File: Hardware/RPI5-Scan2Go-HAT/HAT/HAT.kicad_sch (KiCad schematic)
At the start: 30 parts, among them J1 RPi_GPIO, J10 Screw_Terminal_01x02, J11 Screw_Terminal_01x02, J12 Screw_Terminal_01x02, J13 Screw_Terminal_01x02, J14 Screw_Terminal_01x02, J15 Jack-DC 5V, J16 Screw_Terminal_01x02, J17 Screw_Terminal_01x02, J18 Screw_Terminal_01x02, J2 Screw_Terminal_01x03, J20 Screw_Terminal_01x05, J21 Screw_Terminal_01x06, J3 Conn_01x14_Socket, J4 Screw_Terminal_01x03, J5 Screw_Terminal_01x03, J6 Screw_Terminal_01x03, J7 Screw_Terminal_01x04, J8 Screw_Terminal_01x04, J9 Screw_Terminal_01x02, Q1 DMG2305UX, U1 Pico

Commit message: added footprints
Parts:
- J10, J11, J12, J13, J14, J16, J17, J18, J9: footprint (none) -> TerminalBlock:TerminalBlock_bornier-2_P5.08mm
- J2, J4, J5, J6: footprint (none) -> TerminalBlock:TerminalBlock_bornier-3_P5.08mm
- J20: footprint (none) -> TerminalBlock:TerminalBlock_bornier-5_P5.08mm
- J21: footprint (none) -> TerminalBlock:TerminalBlock_bornier-6_P5.08mm
- J7, J8: footprint (none) -> TerminalBlock:TerminalBlock_bornier-4_P5.08mm
- JP1, JP2: footprint (none) -> Jumper:SolderJumper-2_P1.3mm_Open_TrianglePad1.0x1.5mm
- TP1: footprint (none) -> TestPoint:TestPoint_Pad_2.0x2.0mm
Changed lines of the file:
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@@
 			)
 		)
-		(property "Footprint" ""
+		(property "Footprint" "TerminalBlock:TerminalBlock_bornier-6_P5.08mm"
 			(at 284.48 64.77 0)
 			(effects
@@
 			)
 		)
-		(property "Footprint" ""
+		(property "Footprint" "TerminalBlock:TerminalBlock_bornier-3_P5.08mm"
 			(at 198.12 88.9 0)
 			(effects
@@
 			)
 		)
-		(property "Footprint" ""
+		(property "Footprint" "TerminalBlock:TerminalBlock_bornier-2_P5.08mm"
 			(at 271.78 143.51 0)
 			(effects
@@
 			)
 		)
-		(property "Footprint" ""
+		(property "Footprint" "TerminalBlock:TerminalBlock_bornier-3_P5.08mm"
 			(at 198.12 116.84 0)
 			(effects
@@
 			)
 		)
-		(property "Footprint" ""
+		(property "Footprint" "TerminalBlock:TerminalBlock_bornier-4_P5.08mm"
 			(at 198.12 58.42 0)
 			(effects
@@
 			)
 		)
-		(property "Footprint" ""
+		(property "Footprint" "TerminalBlock:TerminalBlock_bornier-2_P5.08mm"
 			(at 229.87 143.51 0)
 			(effects
@@
 			)
 		)
-		(property "Footprint" ""
+		(property "Footprint" "TerminalBlock:TerminalBlock_bornier-3_P5.08mm"
 			(at 198.12 68.58 0)
 			(effects
@@
 			)
 		)
-		(property "Footprint" ""
+		(property "Footprint" "TestPoint:TestPoint_Pad_2.0x2.0mm"
 			(at 323.85 120.65 0)
 			(effects
@@
 			)
 		)
-		(property "Footprint" ""
+		(property "Footprint" "TerminalBlock:TerminalBlock_bornier-2_P5.08mm"
 			(at 294.64 143.51 0)
 			(effects
@@
 			)
 		)
-		(property "Footprint" ""
+		(property "Footprint" "TerminalBlock:TerminalBlock_bornier-3_P5.08mm"
 			(at 198.12 78.74 0)
 			(effects
@@
 			)
 		)
-		(property "Footprint" ""
+		(property "Footprint" "TerminalBlock:TerminalBlock_bornier-2_P5.08mm"
 			(at 237.49 143.51 0)
 			(effects
@@
 			)
 		)
-		(property "Footprint" ""
+		(property "Footprint" "TerminalBlock:TerminalBlock_bornier-2_P5.08mm"
 			(at 247.65 143.51 0)
 			(effects
@@
 			)
 		)
-		(property "Footprint" ""
+		(property "Footprint" "TerminalBlock:TerminalBlock_bornier-4_P5.08mm"
 			(at 198.12 104.14 0)
 			(effects
@@
 			)
 		)
-		(property "Footprint" ""
+		(property "Footprint" "TerminalBlock:TerminalBlock_bornier-2_P5.08mm"
 			(at 222.25 143.51 0)
 			(effects
@@
 			)
 		)
-		(property "Footprint" ""
+		(property "Footprint" "TerminalBlock:TerminalBlock_bornier-5_P5.08mm"
 			(at 278.13 83.82 0)
 			(effects
@@
 			)
 		)
-		(property "Footprint" ""
+		(property "Footprint" "Jumper:SolderJumper-2_P1.3mm_Open_TrianglePad1.0x1.5mm"
 			(at 100.33 97.79 0)
 			(effects
@@
 			)
 		)
-		(property "Footprint" ""
+		(property "Footprint" "TerminalBlock:TerminalBlock_bornier-2_P5.08mm"
 			(at 214.63 143.51 0)
 			(effects
@@
 			)
 		)
-		(property "Footprint" ""
+		(property "Footprint" "Jumper:SolderJumper-2_P1.3mm_Open_TrianglePad1.0x1.5mm"
 			(at 100.33 102.87 0)
 			(effects
@@
 			)
 		)
-		(property "Footprint" ""
+		(property "Footprint" "TerminalBlock:TerminalBlock_bornier-2_P5.08mm"
 			(at 279.4 143.51 0)
 			(effects
@@
 			)
 		)
-		(property "Footprint" ""
+		(property "Footprint" "TerminalBlock:TerminalBlock_bornier-2_P5.08mm"
 			(at 287.02 143.51 0)
 			(effects

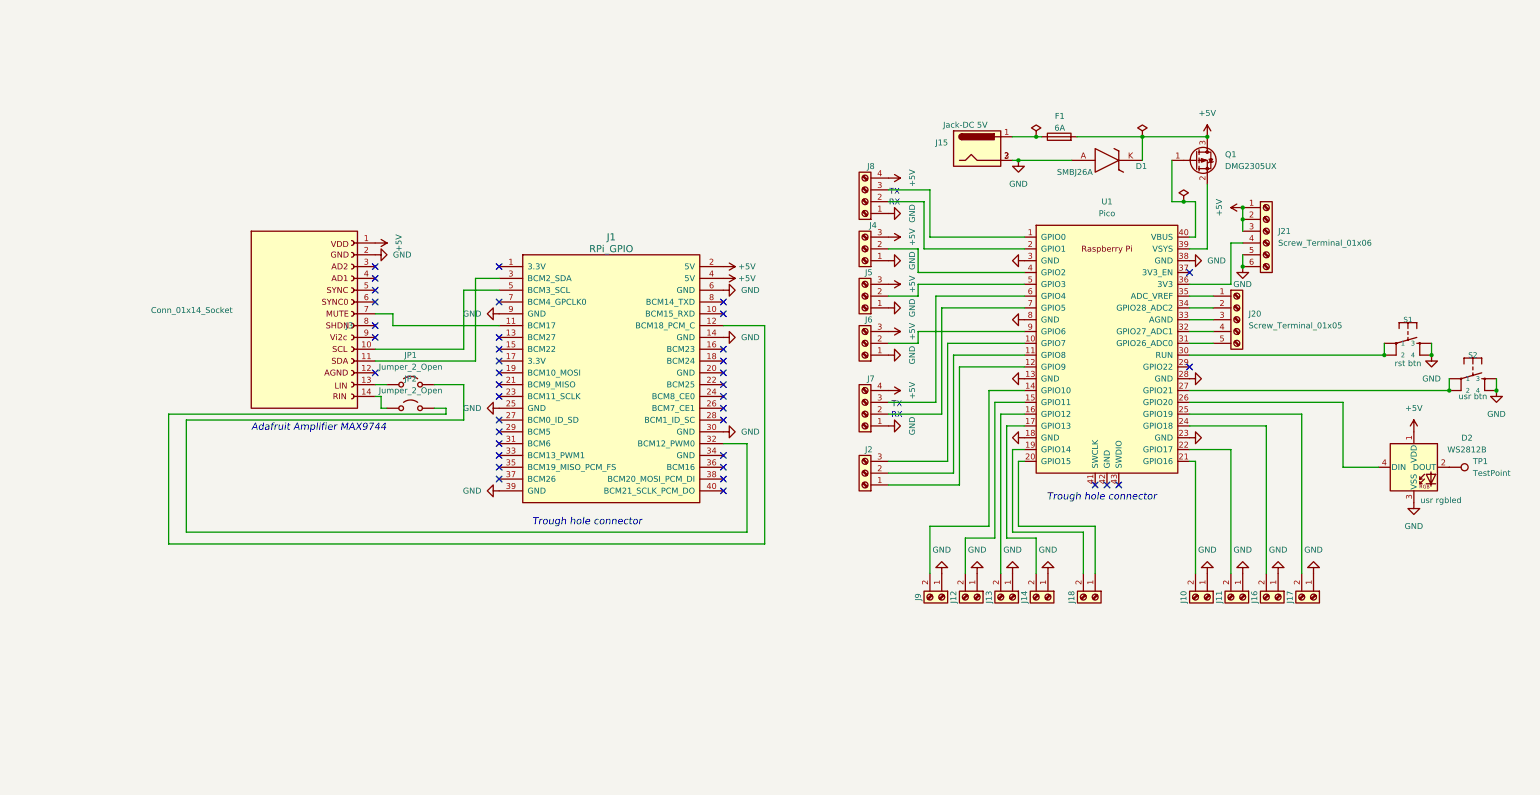
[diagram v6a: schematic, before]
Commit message: changed requirements and pcb format
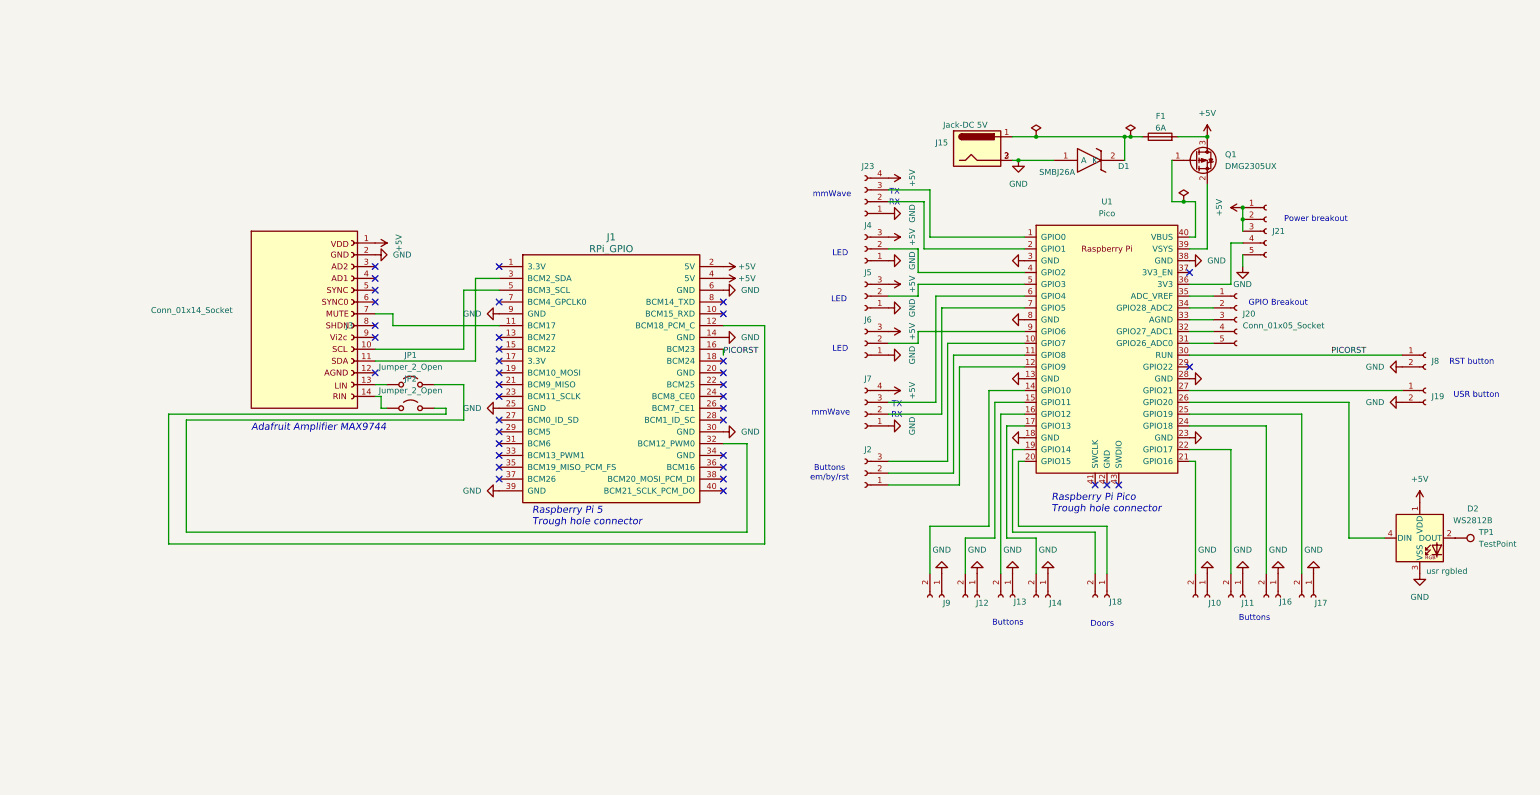
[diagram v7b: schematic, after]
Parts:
- removed J10, J11, J12, J13, J14, J16, J17, J18, J9: Screw_Terminal_01x02, TerminalBlock:TerminalBlock_bornier-2_P5.08mm, symbol Connector:Screw_Terminal_01x02
- removed J2, J4, J5, J6: Screw_Terminal_01x03, TerminalBlock:TerminalBlock_bornier-3_P5.08mm, symbol Connector:Screw_Terminal_01x03
- removed J20: Screw_Terminal_01x05, TerminalBlock:TerminalBlock_bornier-5_P5.08mm, symbol Connector:Screw_Terminal_01x05
- removed J21: Screw_Terminal_01x06, TerminalBlock:TerminalBlock_bornier-6_P5.08mm, symbol Connector:Screw_Terminal_01x06
- removed J7, J8: Screw_Terminal_01x04, TerminalBlock:TerminalBlock_bornier-4_P5.08mm, symbol Connector:Screw_Terminal_01x04
- removed S1, S2: MOMENTARY-SWITCH-SPST-2-SMD-5.2MM, Button_Switch_SMD:SW_SPST_TL3305B, symbol SparkFun-Switches:MOMENTARY-SWITCH-SPST-2-SMD-5.2MM
- added J10, J11, J12, J13, J14, J16, J17, J18, J19, J8, J9: Conn_01x02_Socket, Connector_JST:JST_EH_B3B-EH-A_1x03_P2.50mm_Vertical, symbol Connector:Conn_01x02_Socket
- added J2, J4, J5, J6: Conn_01x03_Socket, Connector_JST:JST_EH_B3B-EH-A_1x03_P2.50mm_Vertical, symbol Connector:Conn_01x03_Socket
- added J20, J21: Conn_01x05_Socket, Connector_JST:JST_EH_B5B-EH-A_1x05_P2.50mm_Vertical, symbol Connector:Conn_01x05_Socket
- added J23, J7: Conn_01x04_Socket, Connector_JST:JST_EH_B4B-EH-A_1x04_P2.50mm_Vertical, symbol Connector:Conn_01x04_Socket
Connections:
- net +5V: now also J21.1 (Pin_1), J21.2 (Pin_2), J21.3 (Pin_3), J23.4 (Pin_4), J4.3 (Pin_3), J5.3 (Pin_3), J6.3 (Pin_3), J7.4 (Pin_4); no longer D1.K
- net GND: now also D1.1 (A), J10.1 (Pin_1), J11.1 (Pin_1), J12.1 (Pin_1), J13.1 (Pin_1), J14.1 (Pin_1), J16.1 (Pin_1), J17.1 (Pin_1), J19.2 (Pin_2), J21.5 (Pin_5), J23.1 (Pin_1), J4.1 (Pin_1), J5.1 (Pin_1), J6.1 (Pin_1), J7.1 (Pin_1), J8.2 (Pin_2), J9.1 (Pin_1); no longer D1.A
- net at U1.36 (3V3): now also J21.4 (Pin_4)
- net at U1.9 (GPIO6): now also J6.2 (Pin_2)
- net at U1.21 (GPIO16): now also J10.2 (Pin_2)
- net at U1.12 (GPIO9): now also J2.1 (Pin_1)
- net at U1.11 (GPIO8): now also J2.2 (Pin_2)
- net at U1.10 (GPIO7): now also J2.3 (Pin_3)
- net at U1.2 (GPIO1): now also J23.2 (Pin_2)
- net at U1.1 (GPIO0): now also J23.3 (Pin_3)
- net at U1.16 (GPIO12): now also J13.2 (Pin_2)
- net at U1.4 (GPIO2): now also J4.2 (Pin_2)
- net at U1.25 (GPIO19): now also J17.2 (Pin_2)
- net at U1.5 (GPIO3): now also J5.2 (Pin_2)
- net at U1.17 (GPIO13): now also J14.2 (Pin_2)
- net at F1.1, J15.1: now also D1.2 (K)
- net at U1.20 (GPIO15): now also J18.1 (Pin_1)
- net at U1.19 (GPIO14): now also J18.2 (Pin_2)
- net PICORST: now reaches J1.16 (BCM23)
- net PICORST: now also U1.30 (RUN), J8.1 (Pin_1)
- net at U1.7 (GPIO5): now also J7.2 (Pin_2)
- net at U1.6 (GPIO4): now also J7.3 (Pin_3)
- net at U1.15 (GPIO11): now also J12.2 (Pin_2)
- net at U1.35 (ADC_VREF): now also J20.1 (Pin_1)
- net at U1.34 (GPIO28_ADC2): now also J20.2 (Pin_2)
- net at U1.33 (AGND): now also J20.3 (Pin_3)
- net at U1.32 (GPIO27_ADC1): now also J20.4 (Pin_4)
- net at U1.31 (GPIO26_ADC0): now also J20.5 (Pin_5)
- net at U1.14 (GPIO10): now also J9.2 (Pin_2)
- net at U1.22 (GPIO17): now also J11.2 (Pin_2)
- net at U1.24 (GPIO18): now also J16.2 (Pin_2)
- net at U1.27 (GPIO21): now also J19.1 (Pin_1)
- no-connect marks 39 -> 38
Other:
- note added: "Buttons"
- note added: "Buttons em/by/rst"
- note added: "Doors"
- note added: "GPIO Breakout"
- note added: "LED"
- note added: "Power breakout"
- note added: "RST button"
- note added: "Raspberry Pi 5 Trough hole connector"
- note added: "Raspberry Pi Pico Trough hole connector"
- note added: "USR button"
- note added: "mmWave"
- note removed: "Trough hole connector"
- moved on the sheet: D2, TP1
